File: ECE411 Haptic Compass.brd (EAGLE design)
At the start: 63.5 x 63.6 mm, 41 parts, among them IC1 SN74LVC1G14DBVR, Q1 PBHV8115TLHR, Q2 PBHV8115TLHR, Q3 PBHV8115TLHR, Q4 PBHV8115TLHR, U1 328P, Y1 ECS-160-8-30Q-VY-TR

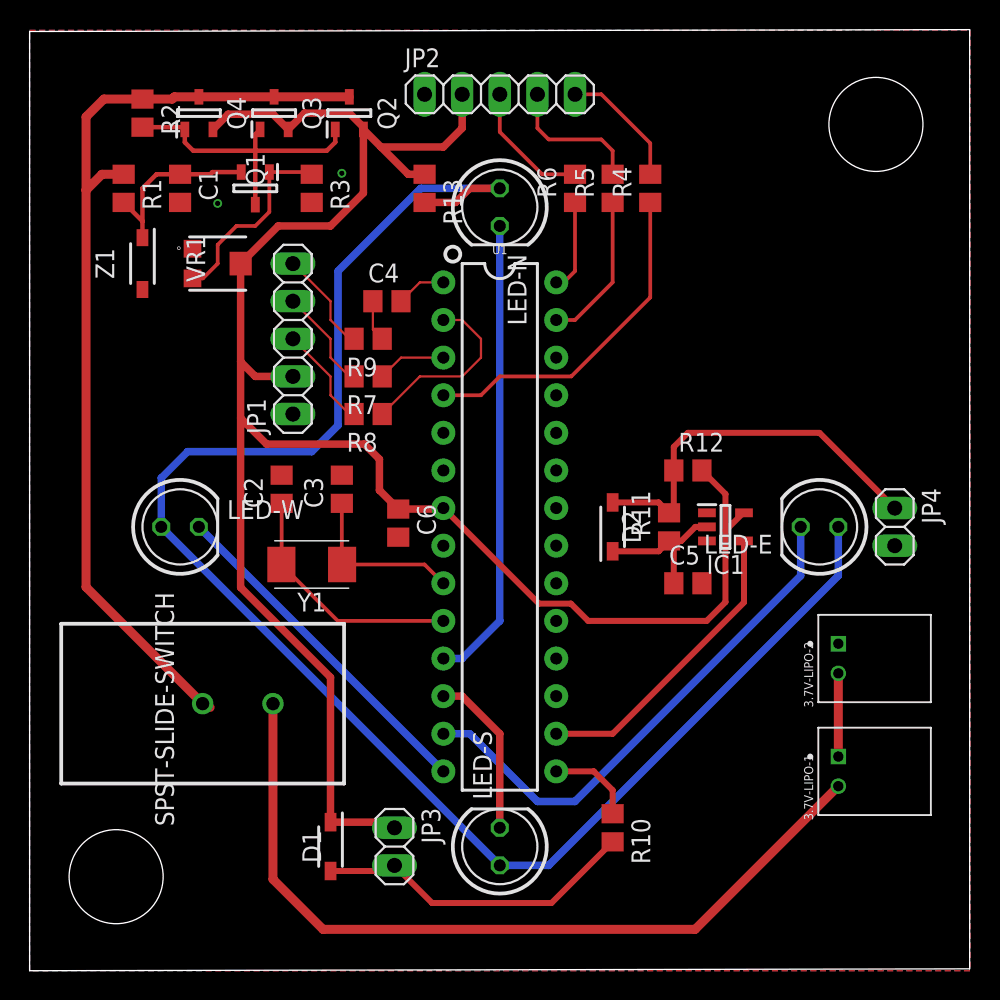
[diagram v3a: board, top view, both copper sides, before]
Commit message: Board Final
Added AVCC, AGND, and VCC bypass capacitors and connected AGND and GND.
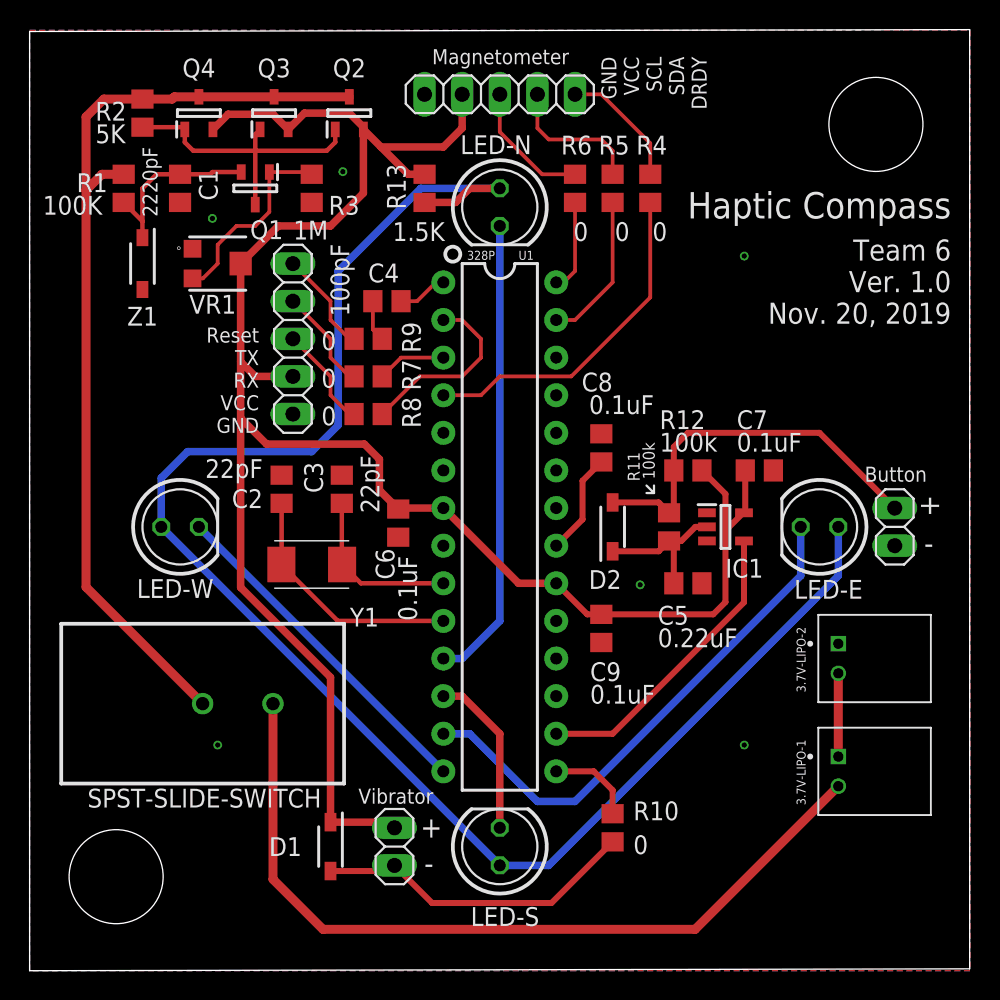
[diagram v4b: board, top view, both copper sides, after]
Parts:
- added C7, C8, C9: 0.1uF, rcl:C0805
- C1: value 220pF -> 2220pF
- C6: value 1uF -> 0.1uF
- R13: value 1500 -> 1.5K
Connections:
- new net VREF: C8.1, U1.21
- net GND: now also C7.2, C8.2, C9.2, U1.22
- net VCC: now also C7.1, C9.1, U1.20
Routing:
- net VREF: track 0.00 -> 6.92 mm
- net VCC: track 140.4 -> 143.0 mm
- net BJT-C: track 64.8 -> 64.2 mm
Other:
- board text added: "+"
- board text added: "-"
- board text added: "Button"
- board text added: "GND VCC SCL SDA DRDY"
- board text added: "Haptic Compass"
- board text added: "Magnetometer"
- board text added: "Reset TX RX VCC GND"
- board text added: "Team 6 Ver. 1.0 Nov. 20, 2019"
- board text added: "Vibrator"

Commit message: Feedback Notes & Final Board
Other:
- board size 63.5 x 63.6 mm -> 63.5 x 63.5 mm
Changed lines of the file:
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@@
 <board>
 <plain>
-<wire x1="0" y1="0" x2="63.48" y2="0.127" width="0" layer="20"/>
-<wire x1="63.48" y1="0.127" x2="63.48" y2="63.551" width="0" layer="20"/>
-<wire x1="63.48" y1="63.551" x2="0" y2="63.424" width="0" layer="20"/>
-<wire x1="0" y1="63.424" x2="0" y2="0" width="0" layer="20"/>
+<wire x1="0" y1="0" x2="63.5054" y2="0.1016" width="0" layer="20"/>
+<wire x1="63.5054" y1="0.1016" x2="63.5054" y2="63.5256" width="0" layer="20"/>
+<wire x1="63.5054" y1="63.5256" x2="0" y2="63.5002" width="0" layer="20"/>
+<wire x1="0" y1="63.5002" x2="0" y2="0" width="0" layer="20"/>
 <hole x="57.15" y="57.15" drill="6.35"/>
 <hole x="5.842" y="6.35" drill="6.35"/>
@@
 <wire x1="42.164" y1="32.258" x2="41.656" y2="32.766" width="0.1524" layer="25"/>
 <text x="27.178" y="61.214" size="1.016" layer="25" font="vector">Magnetometer</text>
+<wire x1="37.592" y1="30.226" x2="37.084" y2="30.226" width="0.1524" layer="21"/>
+<wire x1="37.084" y1="30.226" x2="36.576" y2="30.226" width="0.1524" layer="21"/>
+<wire x1="36.576" y1="30.226" x2="37.084" y2="29.718" width="0.1524" layer="21"/>
+<wire x1="37.084" y1="29.718" x2="37.592" y2="30.226" width="0.1524" layer="21"/>
+<wire x1="36.576" y1="29.718" x2="37.084" y2="29.718" width="0.1524" layer="21"/>
+<wire x1="37.084" y1="29.718" x2="37.592" y2="29.718" width="0.1524" layer="21"/>
+<wire x1="37.084" y1="29.718" x2="37.084" y2="29.21" width="0.1524" layer="21"/>
+<wire x1="37.084" y1="30.226" x2="37.084" y2="30.734" width="0.1524" layer="21"/>
+<wire x1="17.272" y1="8.128" x2="17.78" y2="8.128" width="0.1524" layer="21"/>
+<wire x1="17.78" y1="8.128" x2="18.288" y2="8.128" width="0.1524" layer="21"/>
+<wire x1="18.288" y1="8.128" x2="17.78" y2="8.636" width="0.1524" layer="21"/>
+<wire x1="17.78" y1="8.636" x2="17.272" y2="8.128" width="0.1524" layer="21"/>
+<wire x1="18.288" y1="8.636" x2="17.78" y2="8.636" width="0.1524" layer="21"/>
+<wire x1="17.78" y1="8.636" x2="17.272" y2="8.636" width="0.1524" layer="21"/>
+<wire x1="17.78" y1="8.636" x2="17.78" y2="9.144" width="0.1524" layer="21"/>
+<wire x1="17.78" y1="8.128" x2="17.78" y2="7.62" width="0.1524" layer="21"/>
 </plain>
 <attributes>
@@
 <attribute name="MOUSER_PART_NUMBER" value="841-BAS21GWX" x="-48.26" y="-24.638" size="1.778" layer="27" rot="R270" display="off"/>
 <attribute name="MOUSER_PRICE-STOCK" value="https://www.mouser.com/Search/Refine.aspx?Keyword=841-BAS21GWX" x="-48.26" y="-24.638" size="1.778" layer="27" rot="R270" display="off"/>
-<attribute name="NAME" x="17.272" y="8.382" size="1.27" layer="25" font="vector" align="center"/>
+<attribute name="NAME" x="17.526" y="6.604" size="1.27" layer="25" font="vector" align="center"/>
 </element>
 <element name="D2" library="SamacSys_Parts" package="SOD3616X130N" value="BAS21GWX" x="39.37" y="29.972" smashed="yes" rot="R90">
